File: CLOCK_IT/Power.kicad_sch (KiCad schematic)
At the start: 39 parts, among them J17 Conn_01x04_Socket, Q3 AO3400A, Q4 AO3400A, U19 DS1307N+, U4 AXP2101, Y2 Crystal

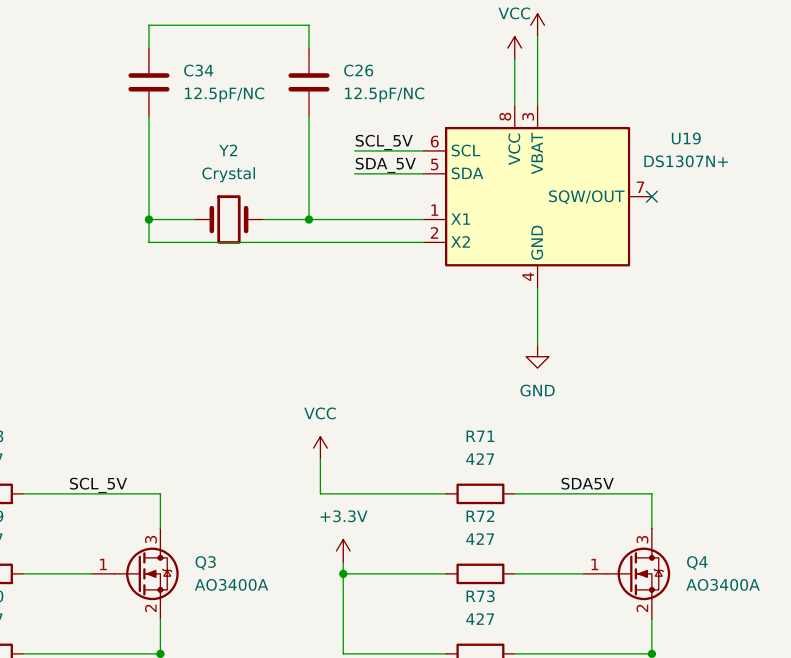
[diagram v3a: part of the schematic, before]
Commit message: :fire: adding I2C communication
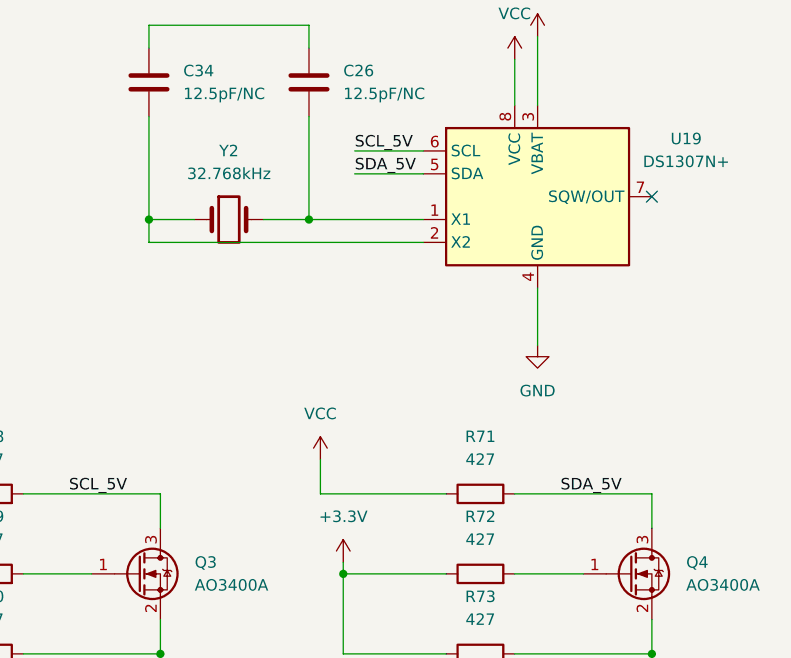
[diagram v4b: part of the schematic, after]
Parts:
- Y2: value Crystal -> 32.768kHz
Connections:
- net SDA5V is gone; now on net SDA_5V: Q4.3 (D), R71.2
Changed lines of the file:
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@@
 		)
 	)
-	(label "SDA5V"
+	(label "SDA_5V"
 		(at 257.81 82.55 0)
 		(effects
@@
 			)
 		)
-		(property "Value" "Crystal"
+		(property "Value" "32.768kHz"
 			(at 220.98 46.99 0)
 			(effects

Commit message: :fire: WORKING ON POWER
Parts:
- removed BT1: Battery_Cell, Battery:BatteryHolder_MPD_BH-18650-PC2, symbol Device:Battery_Cell
- removed C26, C33: 10uF/10V, Capacitor_Tantalum_SMD:CP_EIA-2012-12_Kemet-R, symbol Device:C
- removed C26, C34: 12.5pF/NC, Capacitor_Tantalum_SMD:CP_EIA-2012-12_Kemet-R, symbol Device:C
- removed C28: 22uF/6.3V, symbol Device:C
- removed D17, D18: 1N4148WT, Diode_SMD:D_SOD-523, symbol Diode:1N4148WT
- removed J17: Conn_01x04_Socket, Module:Flipper_Zero_Angled, symbol Connector:Conn_01x04_Socket
- removed L6: 1uH, symbol Device:L
- removed Q3, Q4: AO3400A, Package_TO_SOT_SMD:SOT-23, symbol Transistor_FET:AO3400A
- removed R68, R69, R70, R71, R72, R73: 427, Resistor_SMD:R_01005_0402Metric_Pad0.57x0.30mm_HandSolder, symbol Device:R
- removed U19: DS1307N+, Package_DIP:DIP-8_W7.62mm, symbol Timer_RTC:DS1307N+
- removed Y2: 32.768kHz, Oscillator:Oscillator_SMD_Fox_FT5H_5.0x3.2mm, symbol Device:Crystal
- added R7, R8, R9: 4.7K, symbol Device:R
- added SW1: CK_KMS2xxG, Button_Switch_SMD:SW_SPST_CK_KMS2xxGP, symbol Switch:CK_KMS2xxG
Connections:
- net SCL_5V is gone; now on net GND: U4.40 (SCK)
- net SDA_5V is gone; now on net GND: U4.39 (SDA)
- net GND: now also R7.1, R8.1, R9.1, SW1.2, SW1.SH (B); no longer C30.2
- net MCU 3V3: now also R7.2, R8.2, R9.2
- net VSYS: now also U4.23 (VIN1)
- net at C41.2, U4.6 (VIN3): now also C42.2, U4.7 (VIN4)
- net 3.3V renamed SD_3.3V
- net 5V: no longer names the net of U4.31 (TS)
- net 5V: no longer U4.23 (VIN1)
- net VDCDC2: no longer names the net of U4.26 (FB2)
- new net: C30.2, SW1.1
- no-connect marks 2 -> 7
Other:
- moved on the sheet: C29, C42
